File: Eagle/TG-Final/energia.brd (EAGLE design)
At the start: 172.7 x 172.7 mm, 10 parts, among them IC1 7812T, IC2 7812T, IC3 7806T

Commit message: Fuente 11.1v -> 5v y 3v3
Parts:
- removed D1: 1N4007, adafruit:DO41-10
- added C10, C4, C5, C6, C7, C9: 0.1uf, rcl:C050-024X044
- added C11, C8: 22uf, rcl:E2,5-7
- added C3: 100uf, rcl:E2,5-7
- added JP1: (no value), SparkFun:1X06_LONGPADS
- added L1, L2, L3: 100uH, rcl:0207/7
- added LED1: ROJO, adafruit:LED3MM
- added LED2: VERDE, adafruit:LED3MM
- added Q1: TIP2955, transistor-power:TOP3AV
- added R3: 4K7-2W, rcl:0411/12
- C1: value 470uf -> 0.1uf; device rcl:E3,5-8 -> rcl:C050-024X044
- C2: value 0.1uf -> 470uf; device rcl:C025-025X050 -> rcl:E2,5-7
- IC2: value 7812T -> 7805; device linear:TO220H -> SparkFun:TO-220-ALT
- IC3: value 7806T -> AZ1117; device linear:TO220H -> SparkFun:78XXL
- R1: value 1 Ohm 1W -> 2k2; device rcl:0411/15 -> rcl:0204/5
- R2: value 1 Ohm 1W -> 680; device rcl:0411/15 -> rcl:0204/5
- moved R2 121.5 mm to (-38.1, 125.7)
- moved IC2 87.9 mm to (-105.4, 124.5)
- moved C2 80.0 mm to (-146.1, 135.9), turned to 90 degrees
- moved C1 76.8 mm to (-151.1, 135.9), turned to 90 degrees
- moved R1 76.7 mm to (-81.3, 123.2)
- moved IC3 63.5 mm to (-120.7, 21.6)
- moved U$8 20.7 mm to (-132.1, 87.6), turned to 90 degrees
- moved IC1 7.73 mm to (-114.3, 62.2), turned to 0 degrees
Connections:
- new net N$10: C5.1, IC2.IN, R3.2
- new net N$11: C3.+, C4.1, L1.2, R3.1
- new net N$12: C7.1, C8.+, IC2.OUT, IC3.OUT, L2.2
- new net N$14: LED1.K, R1.1
- new net N$17: C10.1, C11.+, IC3.GND, L3.2
- new net N$18: LED2.K, R2.1
- new net N$3: JP1.5, U$8.14
- new net N$4: JP1.4, U$8.5
- new net N$5: JP1.3, U$8.13
- new net N$6: JP1.2, U$8.12
- new net N$7: U$1.PIN15
- new net N$8: U$1.PIN14
- new net N$9: U$1.PIN13
- net +11V1: now also C1.1, C2.+, L1.1
- net +12V: no longer C1.+, C2.1, D1.A, IC1.3, IC2.3, IC3.1
- net +22V: now also IC1.1, Q1.B, Q1.E; no longer R1.1, R2.1
- net +3V3: now also C9.1, L3.1, LED2.A
- net +6V: no longer IC3.3
- net N$1: now also IC1.3, Q1.C; no longer IC2.1, R2.2
- net N$2: now also JP1.6, U$8.4; no longer D1.C, IC1.1, R1.2
- net VDD: now also C6.1, L2.1, LED1.A; no longer U$8.14
- net VSS: now also C1.2, C10.2, C11.-, C2.-, C3.-, C4.2, C5.2, C6.2, C7.2, C8.-, C9.2, IC2.GND, IC3.IN, R1.2, R2.2; no longer C1.-, C2.2, IC2.2, IC3.2, U$8.5
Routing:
- net +12V: track 147.1 -> 0.00 mm
- net VSS: track 94.4 -> 0.00 mm
- net +6V: track 87.4 -> 0.00 mm
- net +22V: track 37.1 -> 0.00 mm
- net N$2: track 33.3 -> 0.00 mm
- net N$1: track 7.93 -> 0.00 mm

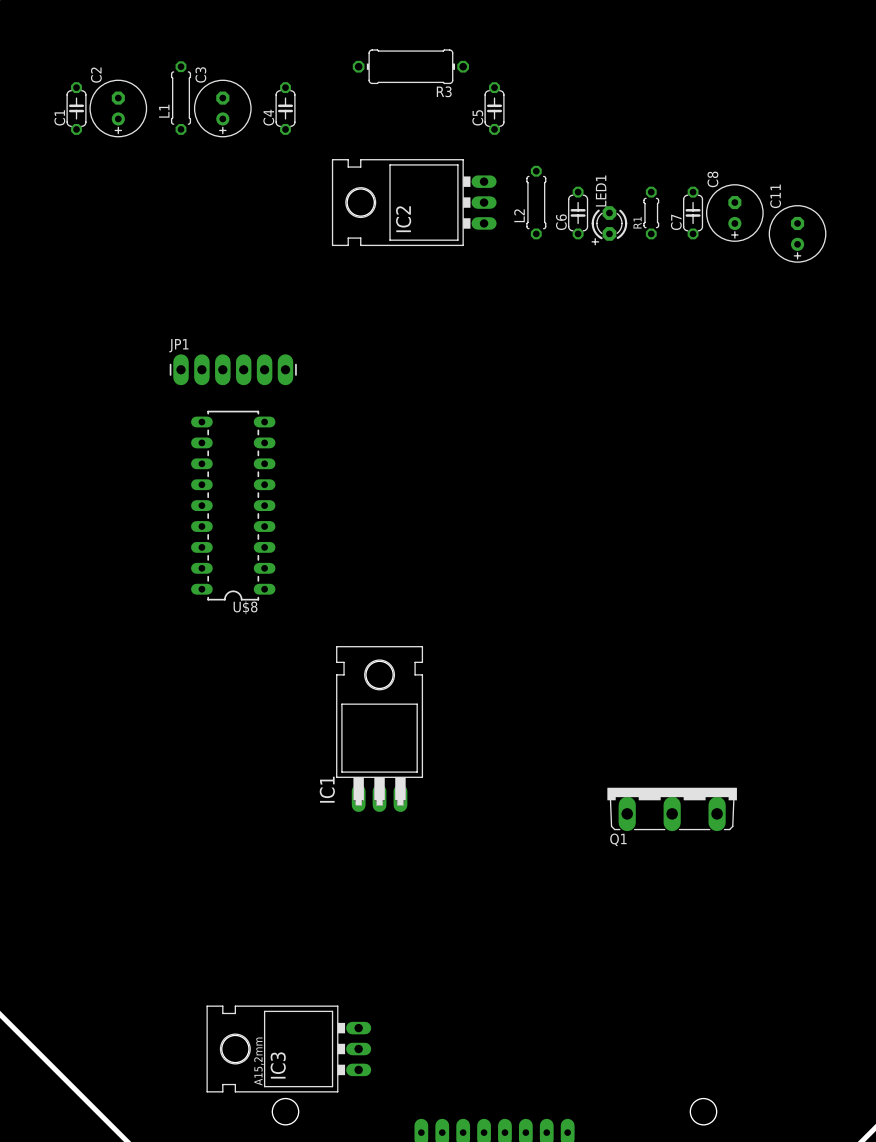
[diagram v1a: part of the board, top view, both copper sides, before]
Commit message: Monitor Baterias LiPO
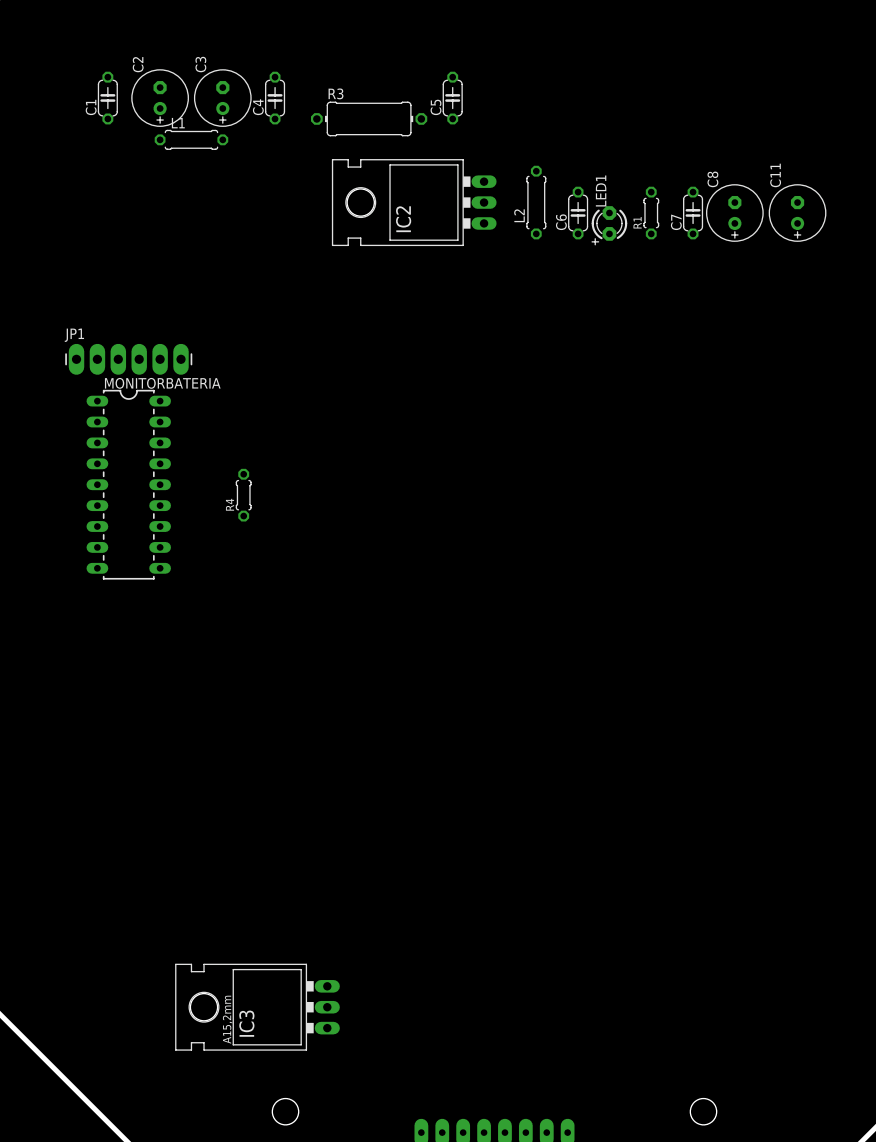
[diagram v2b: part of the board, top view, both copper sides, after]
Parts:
- removed IC1: 7812T, linear:TO220H
- removed Q1: TIP2955, transistor-power:TOP3AV
- removed U$8: PIC16F88-DIP, SparkFun:DIL18
- added MONITORBATERIA: PIC16F88-DIP, SparkFun:DIL18
- added R4: 1k, rcl:0204/5
- JP1: value (none) -> (none)
- moved JP1 12.8 mm to (-151.1, 105.4)
- moved R3 8.13 mm to (-115.6, 134.6), turned to 0 degrees
- moved IC3 6.35 mm to (-124.5, 26.7)
- moved C2 5.24 mm to (-141.0, 137.2)
- moved C5 5.24 mm to (-105.4, 137.2)
- moved L1 5.24 mm to (-137.2, 132.1), turned to 0 degrees
- moved C1 4.02 mm to (-147.3, 137.2)
- moved C11 2.54 mm to (-63.5, 123.2)
- moved C4 1.80 mm to (-127.0, 137.2)
- moved C3 1.27 mm to (-133.3, 137.2)
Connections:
- removed net N$1: IC1.3, Q1.C
- removed net N$3: JP1.5, U$8.14
- removed net N$4: JP1.4, U$8.5
- removed net N$7: U$1.PIN15
- removed net N$8: U$1.PIN14
- removed net N$9: U$1.PIN13
- new net SENSE1: MONITORBATERIA.17, U$1.PIN15
- new net SENSE2: MONITORBATERIA.18, U$1.PIN13
- new net SENSE3: MONITORBATERIA.1, U$1.PIN14
- net +22V: no longer IC1.1, Q1.B, Q1.E
- net N$2: now also MONITORBATERIA.4; no longer U$8.4
- net N$5: now also MONITORBATERIA.13; no longer U$8.13
- net N$6: now also MONITORBATERIA.12; no longer U$8.12
- net VDD: now also JP1.5, MONITORBATERIA.14, R4.1
- net VSS: now also JP1.4, MONITORBATERIA.5, R4.2; no longer IC1.2

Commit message: Fuente de Potencia
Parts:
- removed R3: 4K7-2W, rcl:0411/12
- added C12: 3300uf, rcl:E7,5-18
- added C13, C15: 470uf, rcl:E3,5-8
- added C14: 10uf, rcl:E2,5-5
- added C16, C17: 0.1uf, rcl:C050-024X044
- added D1: 1N4007, diode:DO41-10
- added IC1: 7812T, adafruit:TO220H
- added IC4: 7806T, adafruit:TO220H
- added Q1: TIP2955, transistor-power:TOP3AV
- added R5: 2W100R, rcl:0411/12
- added S1: SWITCH-2-ESTADOS, aasanchez:TL3XYO
- added S2: SWITCH, aasanchez:TL3XYO
- added U$6: 5W0.1RJ, aasanchez:RES-22X10
- added U$9: 10W 5R6J, aasanchez:RES-49X10
- L1: device rcl:0207/7 -> rcl:TFI0307
- moved R4 251.7 mm to (119.4, 61.0), turned to 270 degrees
- moved IC3 238.8 mm to (114.3, 30.5), turned to 0 degrees
- moved IC2 229.7 mm to (104.1, 30.5), turned to 0 degrees
- moved JP1 198.2 mm to (47.0, 100.3), turned to 180 degrees
- moved C2 188.0 mm to (47.0, 137.2)
- moved C4 188.0 mm to (61.0, 137.2)
- moved C6 188.0 mm to (97.8, 123.2)
- moved C7 188.0 mm to (111.8, 123.2)
- moved C8 188.0 mm to (116.8, 123.2)
- moved L3 188.0 mm to (146.1, 121.9)
- moved LED2 188.0 mm to (144.8, 109.2)
- moved R1 188.0 mm to (106.7, 123.2)
- moved R2 188.0 mm to (149.9, 125.7)
- moved C1 188.0 mm to (40.6, 137.2)
- moved C10 188.0 mm to (151.1, 118.1)
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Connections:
- new net N$1: C1.1, C2.+, L1.1, S1.2
- new net N$13: C15.+, C16.1, D1.C, IC4.1
- new net N$4: C12.+, R5.1, S2.2, U$6.P$1
- new net N$7: Q1.E, U$6.P$2
- new net N$8: C13.+, IC1.1, Q1.B, R5.2
- net +11V1: now also S1.1; no longer C1.1, C2.+, L1.1
- net +12V: now also C14.+, D1.A, IC1.3, Q1.C
- net +22V: now also S2.1
- net +6V: now also C17.1, IC4.3
- net N$10: now also U$9.P$2; no longer R3.2
- net N$11: now also U$9.P$1; no longer R3.1
- net VSS: now also C12.-, C13.-, C14.-, C15.-, C16.2, C17.2, IC1.2, IC4.2

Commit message: Trabajos en la Sub Estacion
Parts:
- added C18, C19: 0.1uf, rcl:C050-024X044
- added LED3: ROJO, adafruit:LED3MM
- added LED4: VERDE, adafruit:LED3MM
- added R3: 2k2, rcl:0204/5
- added R6: 680, rcl:0204/5
- S1: value SWITCH-2-ESTADOS -> SWITCH
- moved C11 327.8 mm to (-194.3, 199.4), turned to 0 degrees
- moved LED2 322.9 mm to (-162.6, 208.3), turned to 0 degrees
- moved R2 313.4 mm to (-158.8, 180.3), turned to 0 degrees
- moved C8 309.3 mm to (-182.9, 199.4), turned to 0 degrees
- moved S2 307.4 mm to (-161.3, 34.3), turned to 135 degrees
- moved R4 296.5 mm to (-137.2, 209.6), turned to 0 degrees
- moved LED1 287.6 mm to (-172.7, 208.3), turned to 0 degrees
- moved L2 285.6 mm to (-180.3, 208.3), turned to 0 degrees
- moved U$6 277.4 mm to (-163.8, 67.3), turned to 90 degrees
- moved C13 273.0 mm to (-167.6, 86.4), turned to 270 degrees
- moved C14 270.4 mm to (-157.5, 86.4), turned to 180 degrees
- moved IC1 246.8 mm to (-161.3, 104.1)
- moved R1 244.4 mm to (-121.9, 209.6), turned to 0 degrees
- moved C10 243.9 mm to (-74.9, 209.6), turned to 0 degrees
- moved C9 239.9 mm to (-67.3, 209.6), turned to 0 degrees
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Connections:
- new net N$3: LED3.K, R3.1
- new net N$9: LED4.K, R6.1
- net +11V1: now also S1.3; no longer S1.1
- net +12V: now also C18.1, LED3.A
- net +6V: now also C19.1, LED4.A
- net VSS: now also C18.2, C19.2, R3.2, R6.2
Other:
- board text added: "SUB-ESTACION"

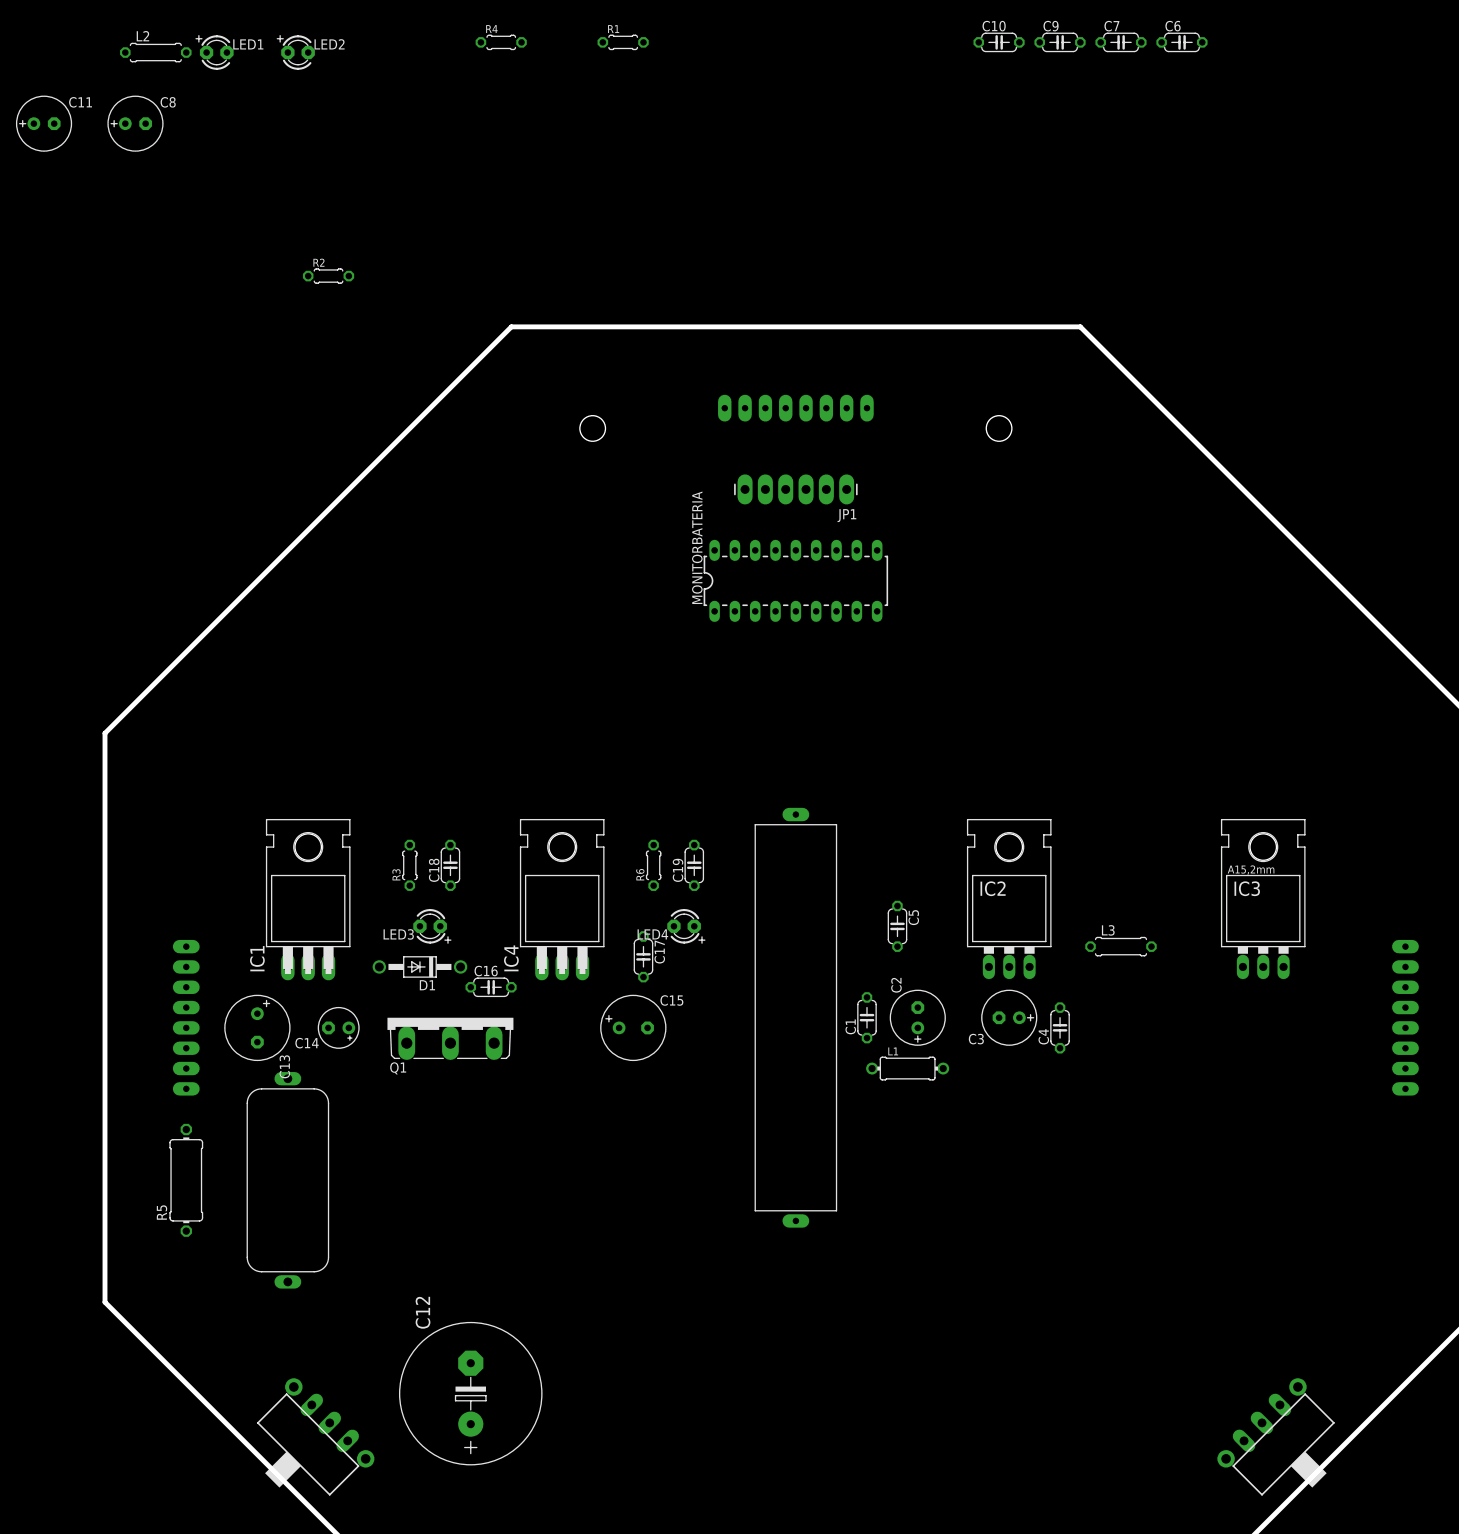
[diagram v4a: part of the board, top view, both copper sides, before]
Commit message: Reposicionando componentes en SubEstación
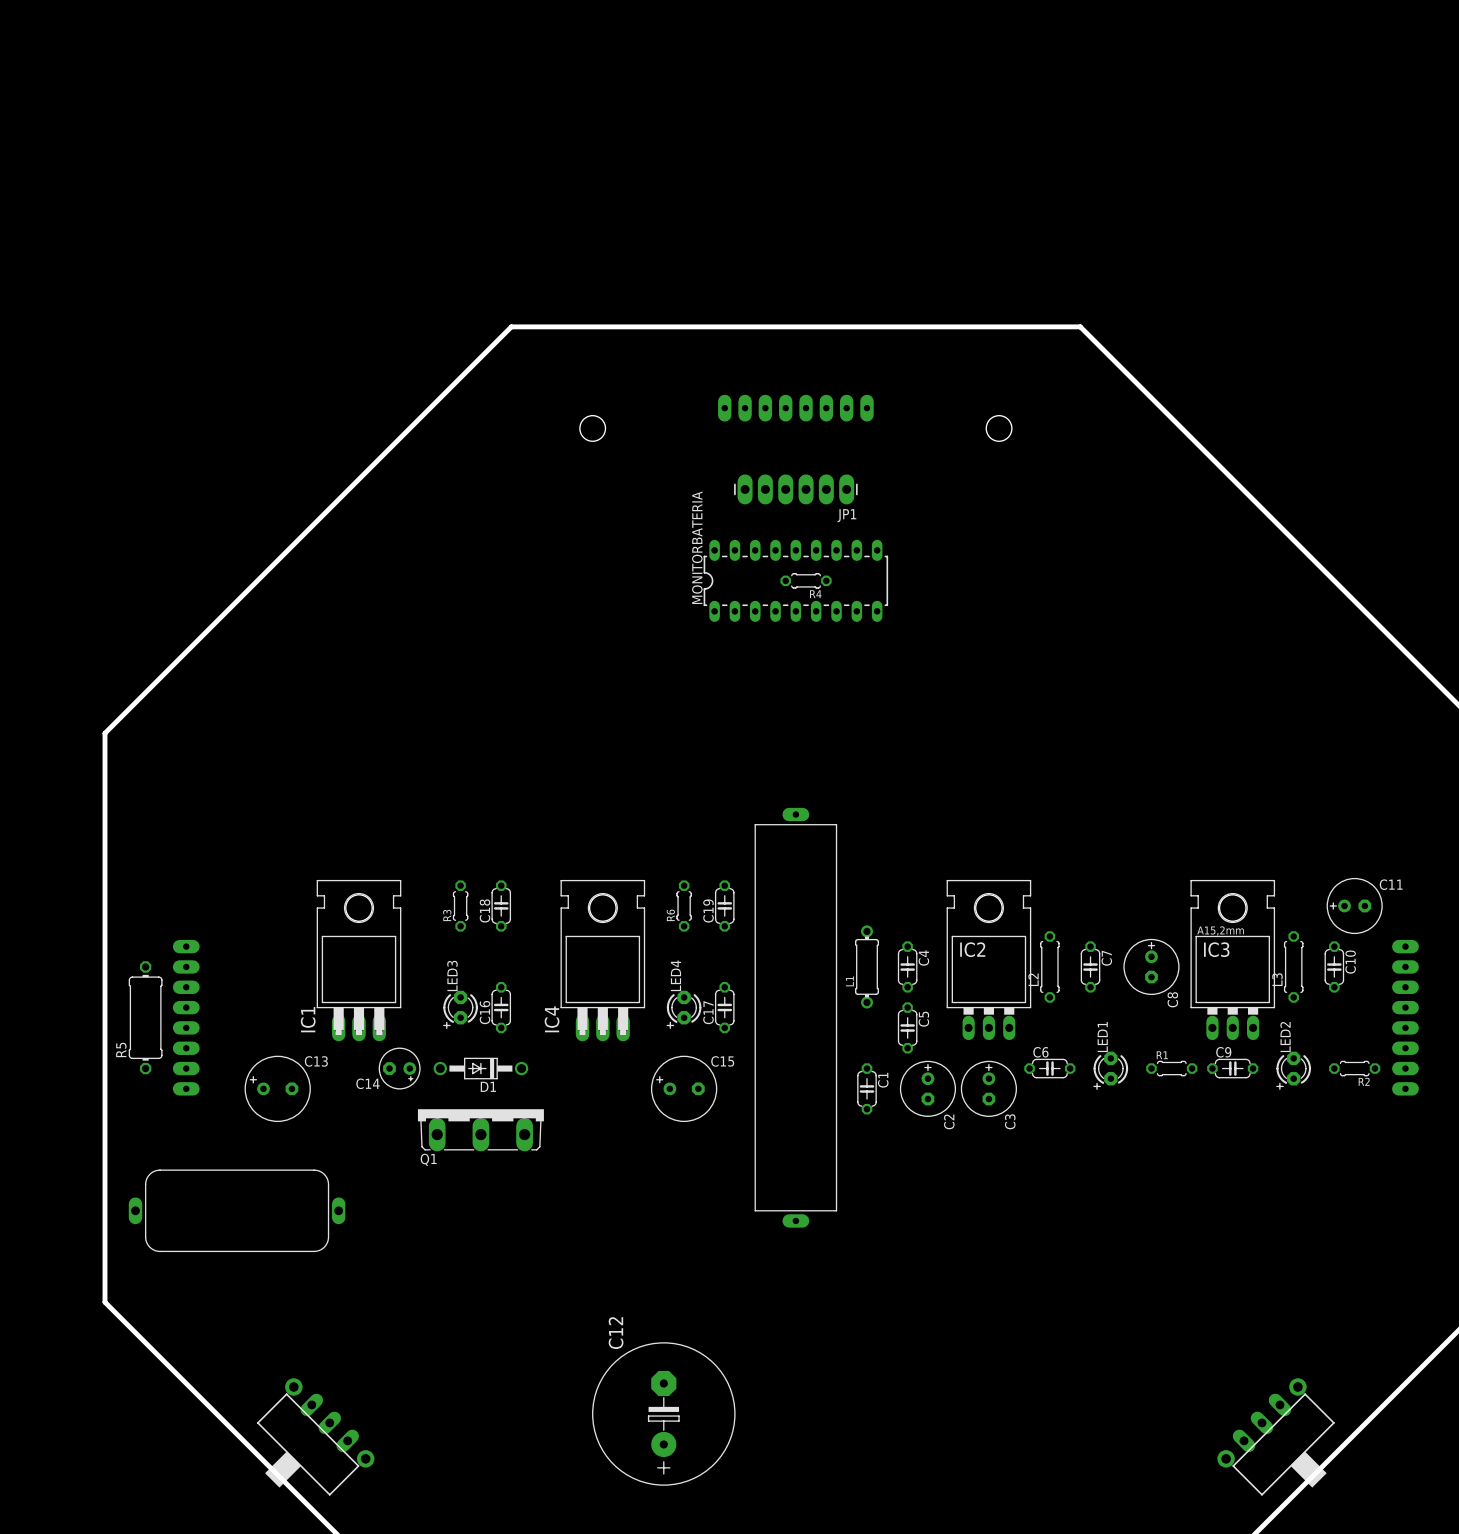
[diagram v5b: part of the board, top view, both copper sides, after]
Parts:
- moved C11 190.8 mm to (-30.5, 101.6)
- moved LED2 177.8 mm to (-38.1, 81.3), turned to 90 degrees
- moved LED1 169.2 mm to (-61.0, 81.3), turned to 90 degrees
- moved C8 165.0 mm to (-55.9, 94.0), turned to 270 degrees
- moved R2 162.1 mm to (-30.5, 81.3), turned to 180 degrees
- moved L2 159.9 mm to (-68.6, 94.0), turned to 90 degrees
- moved R1 145.5 mm to (-53.3, 81.3)
- moved C9 130.1 mm to (-45.7, 81.3)
- moved C6 129.3 mm to (-68.6, 81.3)
- moved C10 122.9 mm to (-33.0, 94.0), turned to 270 degrees
- moved C7 115.6 mm to (-63.5, 94.0), turned to 270 degrees
- moved R4 77.3 mm to (-99.1, 142.2), turned to 180 degrees
- moved C12 24.3 mm to (-116.8, 38.1)
- moved L3 21.7 mm to (-38.1, 94.0), turned to 90 degrees
- moved R5 20.9 mm to (-181.6, 87.6)
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
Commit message: Avanzando....
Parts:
- moved S1 171.0 mm to (88.9, 147.3), turned to 315 degrees
- moved R5 145.9 mm to (-36.8, 69.8), turned to 0 degrees
- moved U$6 137.2 mm to (-33.0, 62.2)
- moved C12 135.9 mm to (19.1, 36.8)
- moved C14 135.9 mm to (-14.0, 80.0)
- moved LED3 135.9 mm to (-6.35, 87.6)
- moved R3 135.9 mm to (-6.35, 100.3)
- moved C1 135.9 mm to (44.5, 77.5), turned to 90 degrees
- moved C13 135.9 mm to (-29.2, 77.5)
- moved C15 135.9 mm to (21.6, 77.5)
- moved C16 135.9 mm to (-1.27, 87.6)
- moved C17 135.9 mm to (26.7, 87.6)
- moved C18 135.9 mm to (-1.27, 100.3)
- moved C19 135.9 mm to (26.7, 100.3)
- moved C6 135.9 mm to (67.3, 80.0)
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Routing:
- net VSS: track 0.00 -> 633.6 mm, vias 0 -> 2
- net +12V: track 0.00 -> 228.7 mm
- net +11V1: track 0.00 -> 213.6 mm
- net VDD: track 0.00 -> 207.7 mm, vias 0 -> 2
- net +6V: track 0.00 -> 148.6 mm
- net N$1: track 0.00 -> 129.1 mm, vias 0 -> 2
- net +3V3: track 0.00 -> 128.3 mm, vias 0 -> 2
- net N$4: track 0.00 -> 92.6 mm
- net N$11: track 0.00 -> 81.0 mm, vias 0 -> 2
- net +22V: track 0.00 -> 72.8 mm
- net SENSE2: track 0.00 -> 64.6 mm
- net N$10: track 0.00 -> 49.9 mm
- net N$12: track 0.00 -> 48.4 mm
- net N$8: track 0.00 -> 44.4 mm
- net SENSE1: track 0.00 -> 36.9 mm
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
